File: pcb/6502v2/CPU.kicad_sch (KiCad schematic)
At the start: 6 parts

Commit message: UART more like u r dumb
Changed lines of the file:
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@@
     (stroke (width 0) (type default) (color 0 0 0 0))
   )
-  (text "CPU" (at 123.5456 146.2024 180)
+  (text "CPU" (at 132.588 137.16 180)
     (effects (font (size 1.27 1.27)) (justify right bottom))
   )

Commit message: just working
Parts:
- J4: renamed from J?; footprint (none) -> Connector_PinHeader_2.54mm:PinHeader_1x02_P2.54mm_Vertical
- gave numbers to parts that had none: 5
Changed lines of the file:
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@@
   (symbol (lib_id "power:+5V") (at 136.144 106.426 0) (unit 1)
     (in_bom yes) (on_board yes)
-    (property "Reference" "#PWR0131" (id 0) (at 136.144 110.236 0)
+    (property "Reference" "#PWR029" (id 0) (at 136.144 110.236 0)
       (effects (font (size 1.27 1.27)) hide)
     )
@@
   (symbol (lib_id "Switch:SW_Push") (at 128.524 68.326 0) (unit 1)
     (in_bom yes) (on_board yes) (fields_autoplaced)
-    (property "Reference" "SW?" (id 0) (at 128.524 60.706 0))
+    (property "Reference" "SW2" (id 0) (at 128.524 60.706 0))
     (property "Value" "SW_Push" (id 1) (at 128.524 63.246 0))
     (property "Footprint" "Button_Switch_SMD:SW_SPST_TL3342" (id 2) (at 128.524 63.246 0)
@@
   (symbol (lib_id "Device:R_Small") (at 136.144 60.706 0) (unit 1)
     (in_bom yes) (on_board yes) (fields_autoplaced)
-    (property "Reference" "R?" (id 0) (at 138.684 59.4359 0)
+    (property "Reference" "R31" (id 0) (at 138.684 59.4359 0)
       (effects (font (size 1.27 1.27)) (justify left))
     )
@@
   (symbol (lib_id "power:+5V") (at 136.144 129.286 0) (unit 1)
     (in_bom yes) (on_board yes) (fields_autoplaced)
-    (property "Reference" "#PWR0130" (id 0) (at 136.144 133.096 0)
+    (property "Reference" "#PWR030" (id 0) (at 136.144 133.096 0)
       (effects (font (size 1.27 1.27)) hide)
     )
@@
   (symbol (lib_id "Device:R_Small") (at 127.254 86.106 0) (unit 1)
     (in_bom yes) (on_board yes) (fields_autoplaced)
-    (property "Reference" "R?" (id 0) (at 129.794 84.8359 0)
+    (property "Reference" "R30" (id 0) (at 129.794 84.8359 0)
       (effects (font (size 1.27 1.27)) (justify left))
     )
@@
   (symbol (lib_id "Device:R_Small") (at 122.174 88.646 0) (unit 1)
     (in_bom yes) (on_board yes) (fields_autoplaced)
-    (property "Reference" "R?" (id 0) (at 124.714 87.3759 0)
+    (property "Reference" "R29" (id 0) (at 124.714 87.3759 0)
       (effects (font (size 1.27 1.27)) (justify left))
     )
@@
   (symbol (lib_id "power:GND") (at 155.194 140.716 0) (unit 1)
     (in_bom yes) (on_board yes) (fields_autoplaced)
-    (property "Reference" "#PWR0132" (id 0) (at 155.194 147.066 0)
+    (property "Reference" "#PWR032" (id 0) (at 155.194 147.066 0)
       (effects (font (size 1.27 1.27)) hide)
     )
@@
   (symbol (lib_id "power:+5V") (at 127.254 83.566 0) (unit 1)
     (in_bom yes) (on_board yes) (fields_autoplaced)
-    (property "Reference" "#PWR0134" (id 0) (at 127.254 87.376 0)
+    (property "Reference" "#PWR027" (id 0) (at 127.254 87.376 0)
       (effects (font (size 1.27 1.27)) hide)
     )
@@
   (symbol (lib_id "power:+5V") (at 155.194 58.166 0) (unit 1)
     (in_bom yes) (on_board yes) (fields_autoplaced)
-    (property "Reference" "#PWR0126" (id 0) (at 155.194 61.976 0)
+    (property "Reference" "#PWR031" (id 0) (at 155.194 61.976 0)
       (effects (font (size 1.27 1.27)) hide)
     )
@@
   (symbol (lib_id "65xx:W65C02SxP") (at 155.194 98.806 0) (unit 1)
     (in_bom yes) (on_board yes) (fields_autoplaced)
-    (property "Reference" "U?" (id 0) (at 157.2134 59.436 0)
+    (property "Reference" "U4" (id 0) (at 157.2134 59.436 0)
       (effects (font (size 1.27 1.27)) (justify left))
     )
@@
   (symbol (lib_id "power:+5V") (at 122.174 86.106 0) (unit 1)
     (in_bom yes) (on_board yes) (fields_autoplaced)
-    (property "Reference" "#PWR0133" (id 0) (at 122.174 89.916 0)
+    (property "Reference" "#PWR026" (id 0) (at 122.174 89.916 0)
       (effects (font (size 1.27 1.27)) hide)
     )
@@
   (symbol (lib_id "Connector_Generic:Conn_01x02") (at 120.904 103.886 180) (unit 1)
     (in_bom yes) (on_board yes) (fields_autoplaced)
-    (property "Reference" "J?" (id 0) (at 120.904 94.8436 0))
+    (property "Reference" "J4" (id 0) (at 120.904 94.8436 0))
     (property "Value" "Conn_01x02" (id 1) (at 120.904 97.3836 0))
-    (property "Footprint" "" (id 2) (at 120.904 103.886 0)
+    (property "Footprint" "Connector_PinHeader_2.54mm:PinHeader_1x02_P2.54mm_Vertical" (id 2) (at 120.904 103.886 0)
       (effects (font (size 1.27 1.27)) hide)
     )
@@
   (symbol (lib_id "power:GND") (at 119.634 68.326 0) (unit 1)
     (in_bom yes) (on_board yes) (fields_autoplaced)
-    (property "Reference" "#PWR0125" (id 0) (at 119.634 74.676 0)
+    (property "Reference" "#PWR025" (id 0) (at 119.634 74.676 0)
       (effects (font (size 1.27 1.27)) hide)
     )
@@
   (symbol (lib_id "power:+5V") (at 136.144 55.626 0) (unit 1)
     (in_bom yes) (on_board yes) (fields_autoplaced)
-    (property "Reference" "#PWR0129" (id 0) (at 136.144 59.436 0)
-      (effects (font (size 1.27 1.27)) hide)
-    )
+    (property "Reference" "#PWR028" (id 0) (at 136.144 59.436 0)
+      (effects (font (size 1.27 1.27)) hide)
+    )

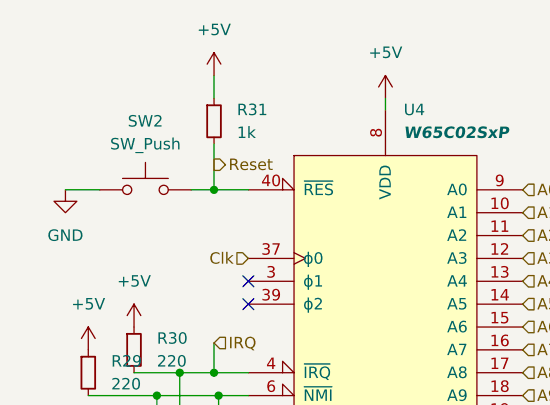
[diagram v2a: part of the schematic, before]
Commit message: Yo yo yo i make the bord 102 by 102 cause jlc pricing
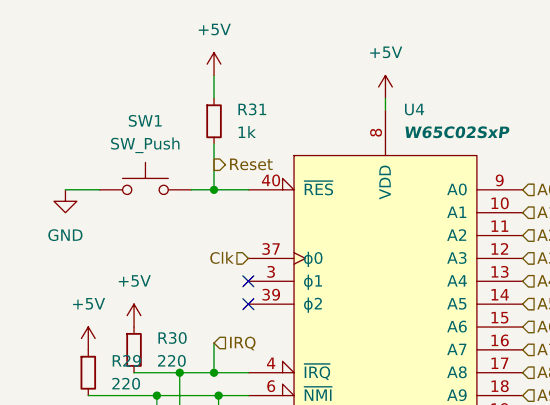
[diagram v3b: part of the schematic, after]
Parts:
- renumbered SW2 to SW1
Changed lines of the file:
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@@
   (symbol (lib_id "power:+5V") (at 136.144 106.426 0) (unit 1)
     (in_bom yes) (on_board yes)
-    (property "Reference" "#PWR029" (id 0) (at 136.144 110.236 0)
+    (property "Reference" "#PWR031" (id 0) (at 136.144 110.236 0)
       (effects (font (size 1.27 1.27)) hide)
     )
@@
   (symbol (lib_id "Switch:SW_Push") (at 128.524 68.326 0) (unit 1)
     (in_bom yes) (on_board yes) (fields_autoplaced)
-    (property "Reference" "SW2" (id 0) (at 128.524 60.706 0))
+    (property "Reference" "SW1" (id 0) (at 128.524 60.706 0))
     (property "Value" "SW_Push" (id 1) (at 128.524 63.246 0))
     (property "Footprint" "Button_Switch_SMD:SW_SPST_TL3342" (id 2) (at 128.524 63.246 0)
@@
   (symbol (lib_id "power:+5V") (at 136.144 129.286 0) (unit 1)
     (in_bom yes) (on_board yes) (fields_autoplaced)
-    (property "Reference" "#PWR030" (id 0) (at 136.144 133.096 0)
+    (property "Reference" "#PWR032" (id 0) (at 136.144 133.096 0)
       (effects (font (size 1.27 1.27)) hide)
     )
@@
   (symbol (lib_id "power:GND") (at 155.194 140.716 0) (unit 1)
     (in_bom yes) (on_board yes) (fields_autoplaced)
-    (property "Reference" "#PWR032" (id 0) (at 155.194 147.066 0)
+    (property "Reference" "#PWR034" (id 0) (at 155.194 147.066 0)
       (effects (font (size 1.27 1.27)) hide)
     )
@@
   (symbol (lib_id "power:+5V") (at 127.254 83.566 0) (unit 1)
     (in_bom yes) (on_board yes) (fields_autoplaced)
-    (property "Reference" "#PWR027" (id 0) (at 127.254 87.376 0)
+    (property "Reference" "#PWR029" (id 0) (at 127.254 87.376 0)
       (effects (font (size 1.27 1.27)) hide)
     )
@@
   (symbol (lib_id "power:+5V") (at 155.194 58.166 0) (unit 1)
     (in_bom yes) (on_board yes) (fields_autoplaced)
-    (property "Reference" "#PWR031" (id 0) (at 155.194 61.976 0)
+    (property "Reference" "#PWR033" (id 0) (at 155.194 61.976 0)
       (effects (font (size 1.27 1.27)) hide)
     )
@@
   (symbol (lib_id "power:+5V") (at 122.174 86.106 0) (unit 1)
     (in_bom yes) (on_board yes) (fields_autoplaced)
-    (property "Reference" "#PWR026" (id 0) (at 122.174 89.916 0)
+    (property "Reference" "#PWR028" (id 0) (at 122.174 89.916 0)
       (effects (font (size 1.27 1.27)) hide)
     )
@@
   (symbol (lib_id "power:GND") (at 119.634 68.326 0) (unit 1)
     (in_bom yes) (on_board yes) (fields_autoplaced)
-    (property "Reference" "#PWR025" (id 0) (at 119.634 74.676 0)
+    (property "Reference" "#PWR027" (id 0) (at 119.634 74.676 0)
       (effects (font (size 1.27 1.27)) hide)
     )
@@
   (symbol (lib_id "power:+5V") (at 136.144 55.626 0) (unit 1)
     (in_bom yes) (on_board yes) (fields_autoplaced)
-    (property "Reference" "#PWR028" (id 0) (at 136.144 59.436 0)
-      (effects (font (size 1.27 1.27)) hide)
-    )
+    (property "Reference" "#PWR030" (id 0) (at 136.144 59.436 0)
+      (effects (font (size 1.27 1.27)) hide)
+    )

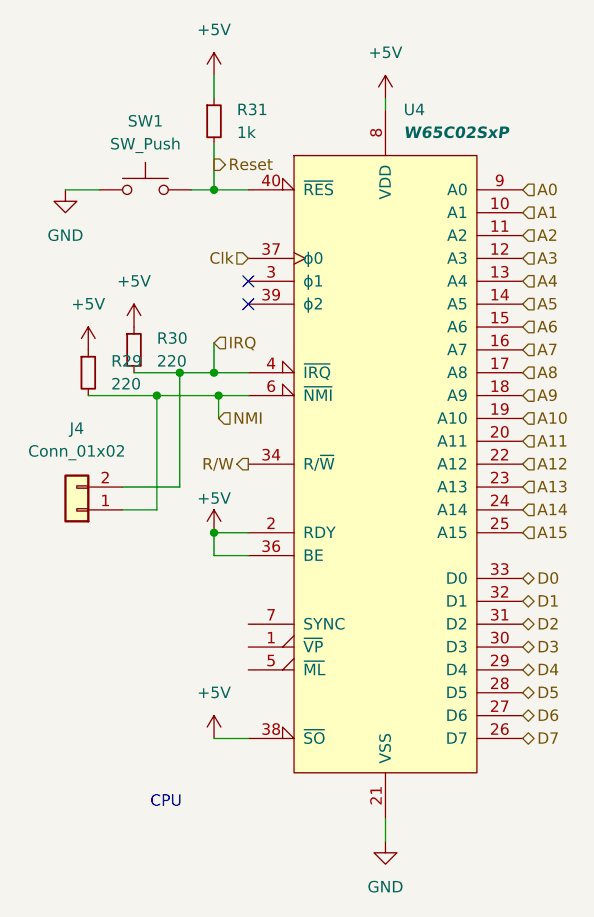
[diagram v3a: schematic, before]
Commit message: First pass at routing done, now comes double checking everything
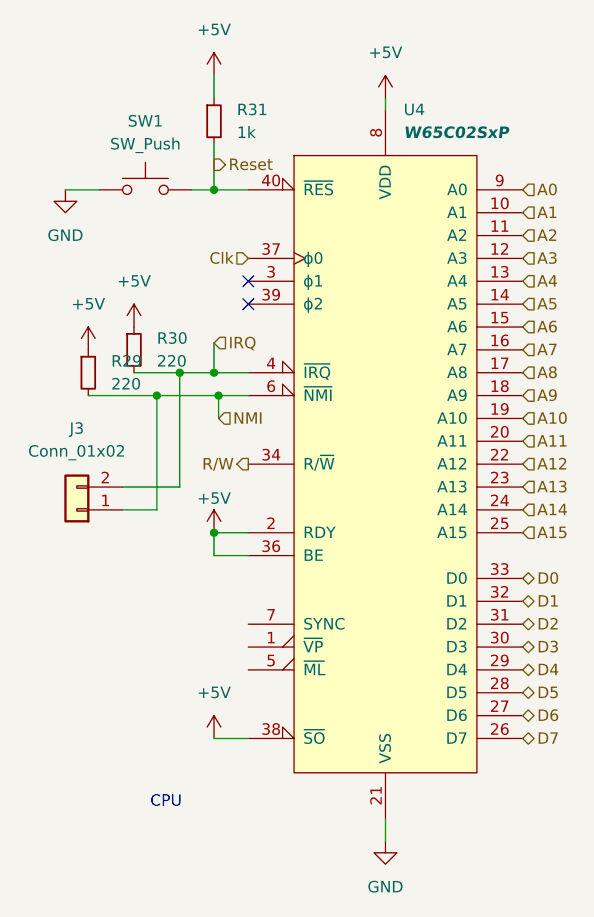
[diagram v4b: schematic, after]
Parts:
- renumbered J4 to J3
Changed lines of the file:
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@@
   (symbol (lib_id "power:+5V") (at 136.144 106.426 0) (unit 1)
     (in_bom yes) (on_board yes)
-    (property "Reference" "#PWR031" (id 0) (at 136.144 110.236 0)
+    (property "Reference" "#PWR034" (id 0) (at 136.144 110.236 0)
       (effects (font (size 1.27 1.27)) hide)
     )
@@
   (symbol (lib_id "power:+5V") (at 136.144 129.286 0) (unit 1)
     (in_bom yes) (on_board yes) (fields_autoplaced)
-    (property "Reference" "#PWR032" (id 0) (at 136.144 133.096 0)
+    (property "Reference" "#PWR035" (id 0) (at 136.144 133.096 0)
       (effects (font (size 1.27 1.27)) hide)
     )
@@
   (symbol (lib_id "power:GND") (at 155.194 140.716 0) (unit 1)
     (in_bom yes) (on_board yes) (fields_autoplaced)
-    (property "Reference" "#PWR034" (id 0) (at 155.194 147.066 0)
+    (property "Reference" "#PWR037" (id 0) (at 155.194 147.066 0)
       (effects (font (size 1.27 1.27)) hide)
     )
@@
   (symbol (lib_id "power:+5V") (at 127.254 83.566 0) (unit 1)
     (in_bom yes) (on_board yes) (fields_autoplaced)
-    (property "Reference" "#PWR029" (id 0) (at 127.254 87.376 0)
+    (property "Reference" "#PWR032" (id 0) (at 127.254 87.376 0)
       (effects (font (size 1.27 1.27)) hide)
     )
@@
   (symbol (lib_id "power:+5V") (at 155.194 58.166 0) (unit 1)
     (in_bom yes) (on_board yes) (fields_autoplaced)
-    (property "Reference" "#PWR033" (id 0) (at 155.194 61.976 0)
+    (property "Reference" "#PWR036" (id 0) (at 155.194 61.976 0)
       (effects (font (size 1.27 1.27)) hide)
     )
@@
   (symbol (lib_id "power:+5V") (at 122.174 86.106 0) (unit 1)
     (in_bom yes) (on_board yes) (fields_autoplaced)
-    (property "Reference" "#PWR028" (id 0) (at 122.174 89.916 0)
+    (property "Reference" "#PWR031" (id 0) (at 122.174 89.916 0)
       (effects (font (size 1.27 1.27)) hide)
     )
@@
   (symbol (lib_id "Connector_Generic:Conn_01x02") (at 120.904 103.886 180) (unit 1)
     (in_bom yes) (on_board yes) (fields_autoplaced)
-    (property "Reference" "J4" (id 0) (at 120.904 94.8436 0))
+    (property "Reference" "J3" (id 0) (at 120.904 94.8436 0))
     (property "Value" "Conn_01x02" (id 1) (at 120.904 97.3836 0))
     (property "Footprint" "Connector_PinHeader_2.54mm:PinHeader_1x02_P2.54mm_Vertical" (id 2) (at 120.904 103.886 0)
@@
   (symbol (lib_id "power:GND") (at 119.634 68.326 0) (unit 1)
     (in_bom yes) (on_board yes) (fields_autoplaced)
-    (property "Reference" "#PWR027" (id 0) (at 119.634 74.676 0)
+    (property "Reference" "#PWR030" (id 0) (at 119.634 74.676 0)
       (effects (font (size 1.27 1.27)) hide)
     )
@@
   (symbol (lib_id "power:+5V") (at 136.144 55.626 0) (unit 1)
     (in_bom yes) (on_board yes) (fields_autoplaced)
-    (property "Reference" "#PWR030" (id 0) (at 136.144 59.436 0)
-      (effects (font (size 1.27 1.27)) hide)
-    )
+    (property "Reference" "#PWR033" (id 0) (at 136.144 59.436 0)
+      (effects (font (size 1.27 1.27)) hide)
+    )
